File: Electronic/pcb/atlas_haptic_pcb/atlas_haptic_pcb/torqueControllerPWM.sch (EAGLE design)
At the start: 8 parts, among them U1 ISO1541, U2 NUCLEO-L053R8, U3 MCP4725

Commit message: PWM schematic contd.
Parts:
- U2: value NUCLEO-L053R8 -> NUCLEO-F410RE; device NUCLEO-L053R8:NUCLEO-L053R8 -> NUCLEO-L053R8:NUCLEO-F410RE
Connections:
- net BIASED_VOLTAGE: now also U2CN7.PA0/A0
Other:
- moved on the sheet: U2CN10, U2CN7
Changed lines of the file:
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@@
 <part name="SUPPLY8" library="SparkFun-PowerSymbols" library_urn="urn:adsk.eagle:library:530" deviceset="5V" device=""/>
 <part name="SUPPLY5" library="SparkFun-PowerSymbols" library_urn="urn:adsk.eagle:library:530" deviceset="5V" device=""/>
-<part name="U2" library="NUCLEO-L053R8" deviceset="NUCLEO-L053R8" device=""/>
+<part name="U2" library="NUCLEO-L053R8" deviceset="NUCLEO-F410RE" device=""/>
 </parts>
 <sheets>
@@
 <instance part="SUPPLY8" gate="G$1" x="63.5" y="58.42"/>
 <instance part="SUPPLY5" gate="G$1" x="30.48" y="86.36"/>
-<instance part="U2" gate="CN7" x="152.4" y="73.66"/>
-<instance part="U2" gate="CN10" x="210.82" y="73.66"/>
+<instance part="U2" gate="CN7" x="157.48" y="68.58"/>
+<instance part="U2" gate="CN10" x="226.06" y="68.58"/>
 </instances>
 <busses>
@@
 <wire x1="58.42" y1="50.8" x2="63.5" y2="50.8" width="0.1524" layer="91"/>
 <label x="63.5" y="50.8" size="1.778" layer="95"/>
+<wire x1="63.5" y1="50.8" x2="116.84" y2="50.8" width="0.1524" layer="91"/>
+<wire x1="116.84" y1="50.8" x2="116.84" y2="35.56" width="0.1524" layer="91"/>
+<wire x1="116.84" y1="35.56" x2="193.04" y2="35.56" width="0.1524" layer="91"/>
+<wire x1="193.04" y1="35.56" x2="193.04" y2="58.42" width="0.1524" layer="91"/>
+<pinref part="U2" gate="CN7" pin="PA0/A0"/>
+<wire x1="193.04" y1="58.42" x2="177.8" y2="58.42" width="0.1524" layer="91"/>
 </segment>
 </net>

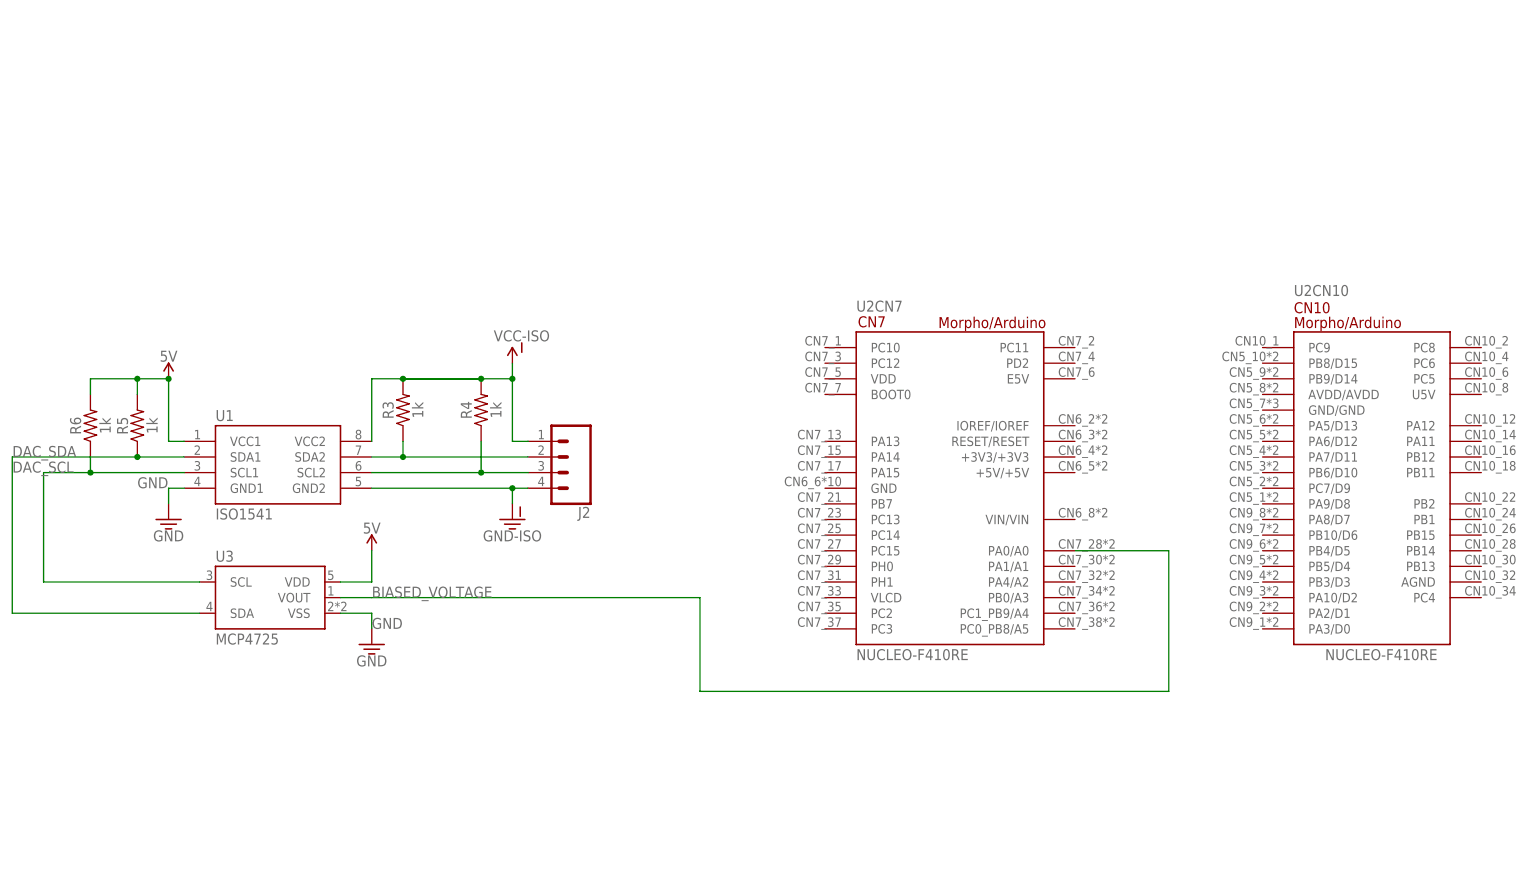
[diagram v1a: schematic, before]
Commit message: PWM torque controller is added.
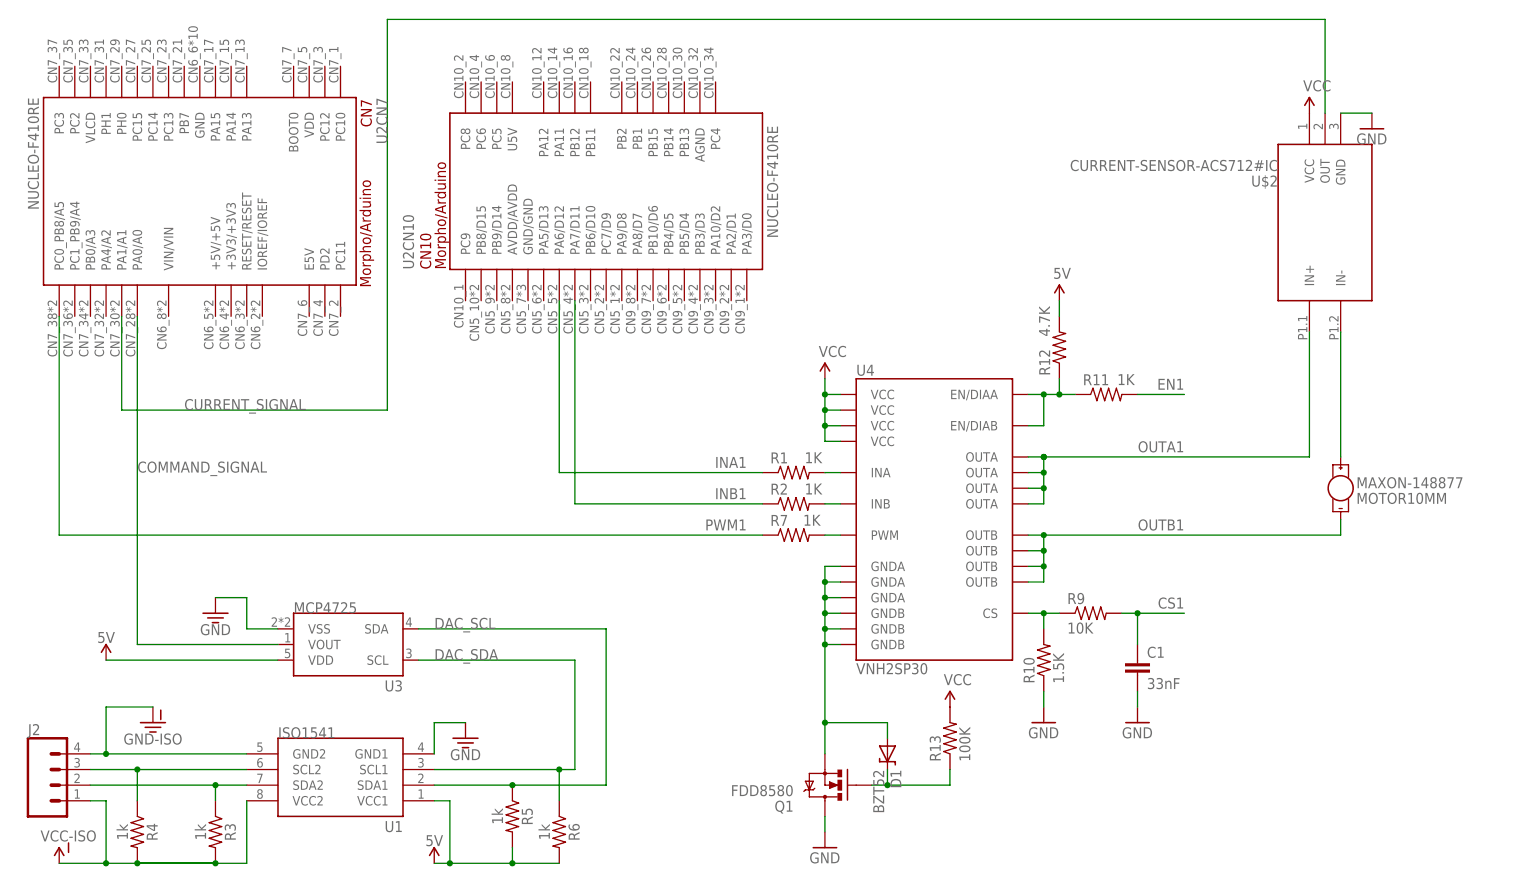
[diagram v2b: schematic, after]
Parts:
- added C1: 33nF, SparkFun:CAP0402-CAP
- added D1: BZT52, SparkFun:DIODE-ZENER-BZT52
- added MAXON-148877: MOTOR10MM, SparkFun-Electromechanical:MOTOR10MM
- added Q1: FDD8580, SparkFun:MOSFET-NCHANNELFDD8580
- added R1, R11, R2, R7: 1K, SparkFun:RESISTOR0402-RES
- added R10: 1.5K, SparkFun:RESISTOR0402-RES
- added R12: 4.7K, SparkFun:RESISTOR0402-RES
- added R13: 100K, SparkFun:RESISTOR0402-RES
- added R9: 10K, SparkFun:RESISTOR0402-RES
- added U$2: CURRENT-SENSOR-ACS712#IC, acs712:CURRENT-SENSOR-ACS712#IC
- added U4: VNH2SP30, SparkFun:VNH2SP30
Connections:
- net BIASED_VOLTAGE renamed COMMAND_SIGNAL
- new net 3.3V: U3.VSS
- new net CS1: C1.1, R9.2
- new net CURRENT_SIGNAL: U$2.OUT, U2CN7.PA1/A1
- new net EN1: R11.2
- new net INA1: R1.1, U2CN10.PA6/D12
- new net INB1: R2.1, U2CN10.PA7/D11
- new net N$1: R2.2, U4.INB
- new net N$10: D1.A, Q1.S, U4.GNDA@26, U4.GNDA@27, U4.GNDA@28, U4.GNDB@18, U4.GNDB@19, U4.GNDB@20
- new net N$12: R11.1, R12.1, U4.EN/DIAA, U4.EN/DIAB
- new net N$13: D1.C, Q1.G, R13.1
- new net N$2: R1.2, U4.INA
- new net N$5: R7.2, U4.PWM
- new net N$7: R10.2, R9.1, U4.CS
- new net N$8: MAXON-148877.+, U$2.IN-
- new net OUTA1: U$2.IN+, U4.OUTA@1, U4.OUTA@25, U4.OUTA@30, U4.OUTA@SLUG3
- new net OUTB1: MAXON-148877.-, U4.OUTB@15, U4.OUTB@16, U4.OUTB@21, U4.OUTB@SLUG2
- new net PWM1: R7.1, U2CN7.PC0_PB8/A5
- new net VCC: R13.2, U$2.VCC, U4.VCC@13, U4.VCC@23, U4.VCC@3, U4.VCC@SLUG1
- net 5V: now also R12.2
- net GND: now also C1.2, Q1.D, R10.1, U$2.GND; no longer U3.VSS
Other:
- moved on the sheet: J2, R3, R4, R5, R6, U1, U2CN10, U2CN7, U3
